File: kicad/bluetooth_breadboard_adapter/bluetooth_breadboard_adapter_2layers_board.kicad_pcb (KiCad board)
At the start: 2 copper layers, 24.9 x 36.1 mm, 5 parts, among them J1 SCJ368R1NUS0B00G, P1 CONNECTOR, P2 CONNECTOR, U1 BLK-MD-SPK-B

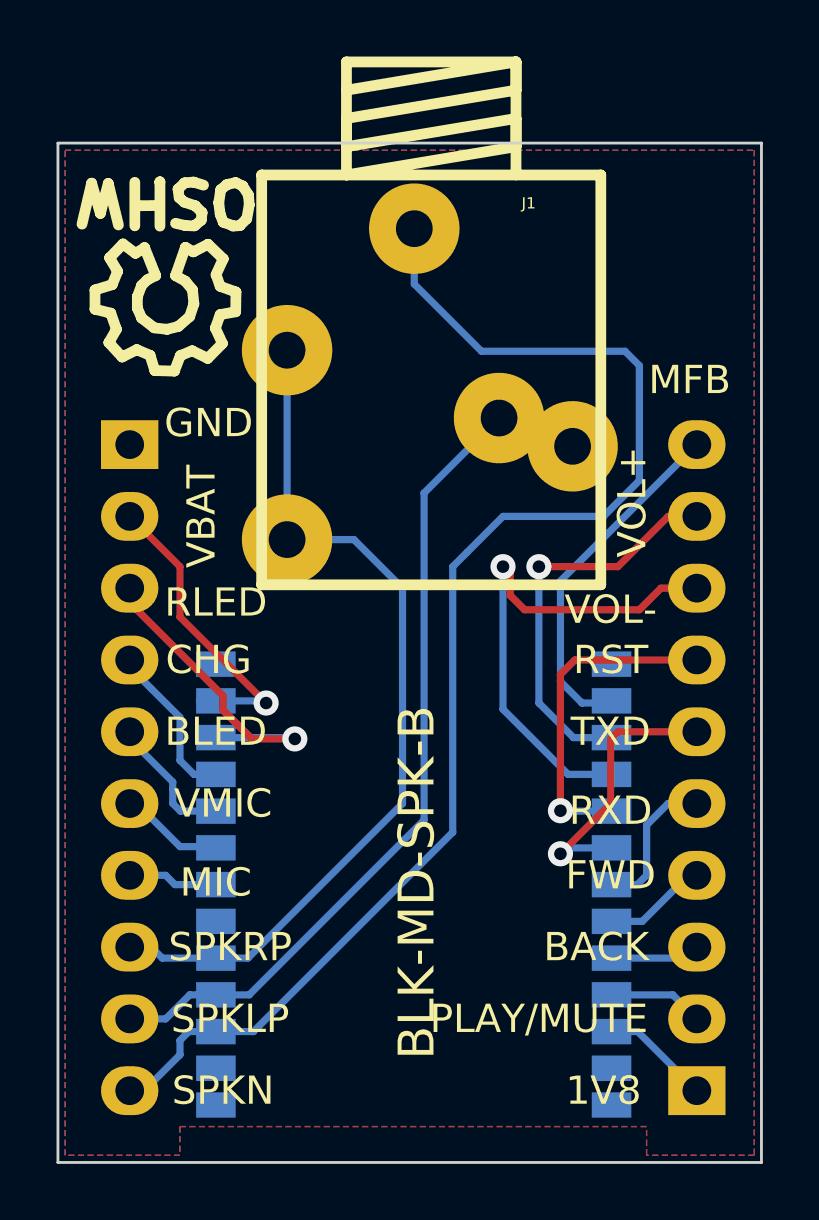
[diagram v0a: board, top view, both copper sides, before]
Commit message: 3.5mm jack update to scj-0354-5PU
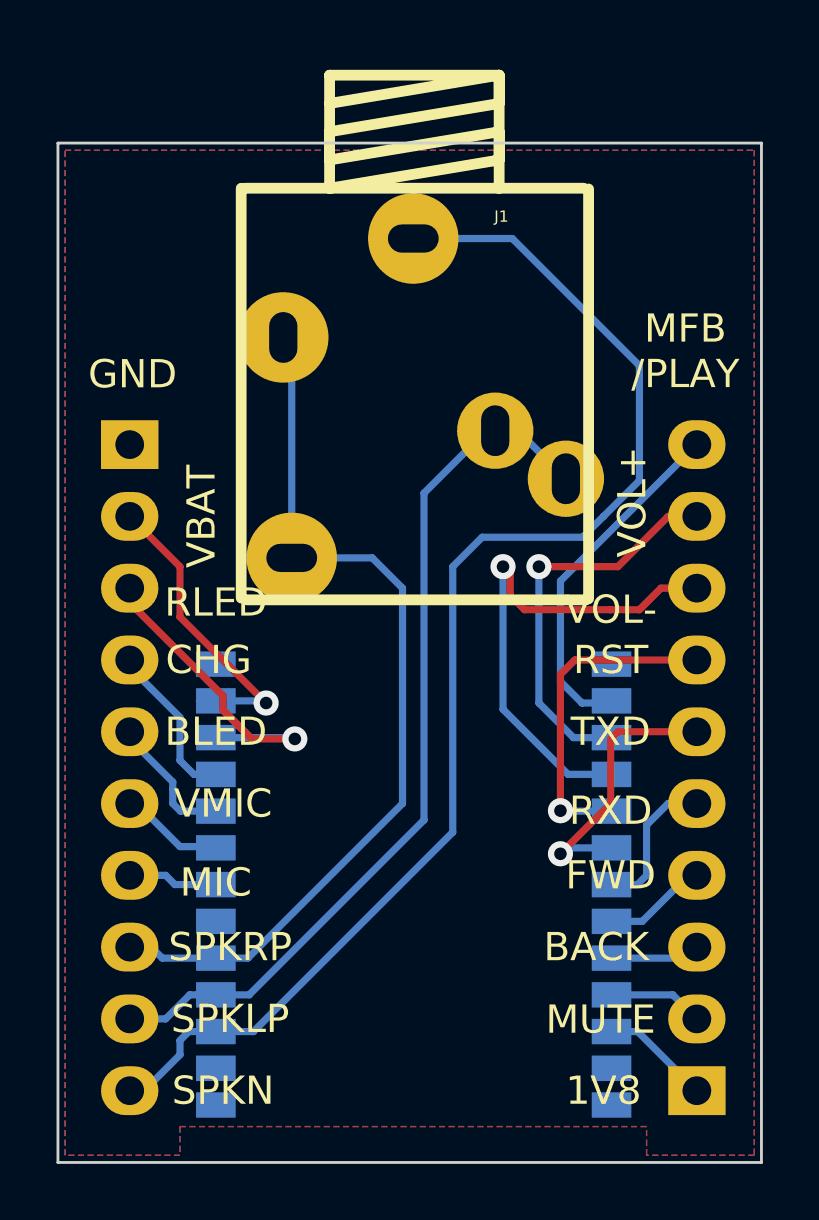
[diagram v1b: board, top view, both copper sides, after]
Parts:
- removed SYM: Symbol_OSHW-Logo_SilkScreen_07Jul2012, Symbols:Symbol_OSHW-Logo_SilkScreen
- J1: value SCJ368R1NUS0B00G -> SCJ-0354-5PU; footprint 3.5mm stereo jack:3.5mm_stereo_jack -> jacks:SCJ-0354-5PU
- U1: footprint BLK-MD-SPK-B:BLK-MD-SPK-B -> my_modules:BLK-MD-SPK-B
- moved J1 6.48 mm to (221.1, 131.0)
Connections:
- P2 pad 8: Net-(J1-Pad2) -> Net-(J1-Pad4)
- P2 pad 9: Net-(J1-Pad4) -> Net-(J1-Pad2)
- U1 pad 4: Net-(J1-Pad4) -> Net-(J1-Pad2)
- U1 pad 5: Net-(J1-Pad2) -> Net-(J1-Pad4)
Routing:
- net Net-(J1-Pad1): track 48.3 -> 47.0 mm
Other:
- board text added: "MFB /PLAY"
- board text added: "MUTE"
- board text removed: "MFB"
- board text removed: "PLAY/MUTE"
